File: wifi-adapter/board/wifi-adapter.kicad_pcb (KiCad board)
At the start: 2 copper layers, 25 x 24 mm, 17 parts, among them J1 DF13A-6P-1.25H, U1 LM1117IMPX-3.3, U2 ESP-07

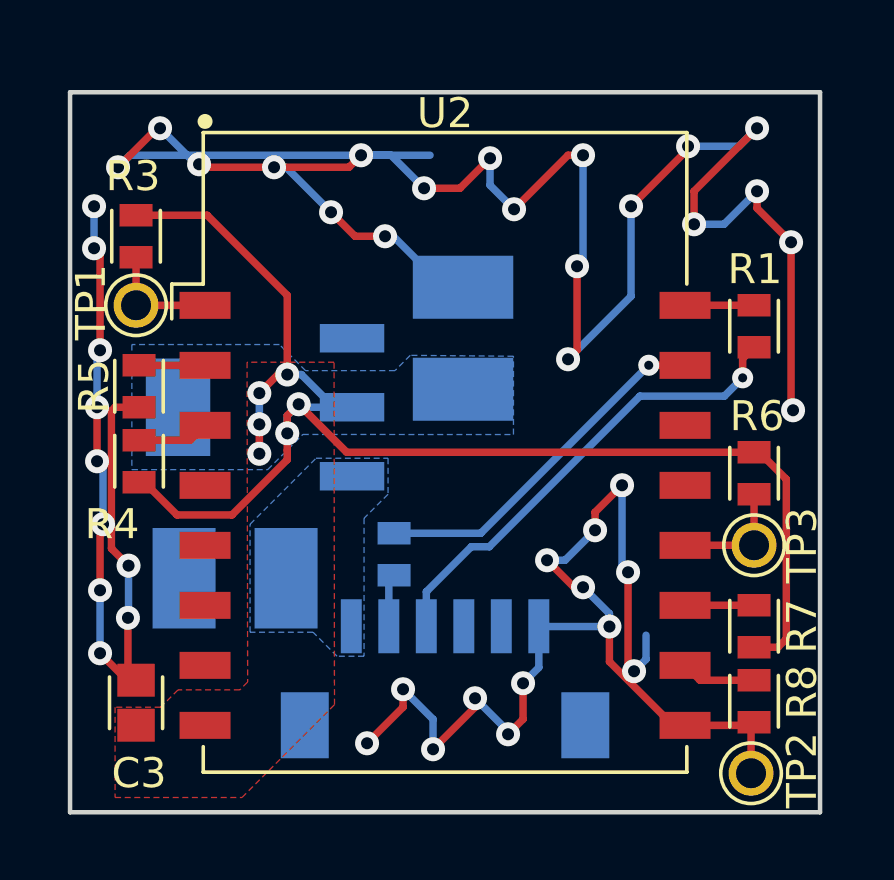
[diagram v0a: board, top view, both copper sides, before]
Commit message: Add GOST style schematic and gerber files
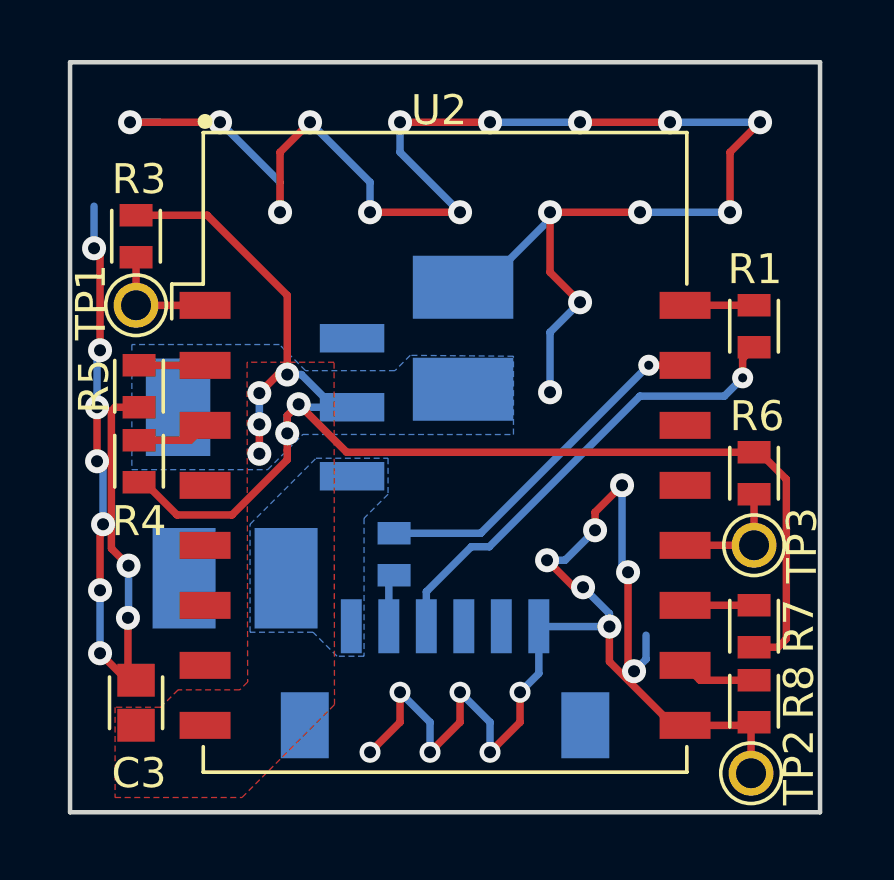
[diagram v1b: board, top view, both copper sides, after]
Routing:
- net GND: track 136.5 -> 122.3 mm, vias 43 -> 38
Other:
- board size 25 x 24 mm -> 25 x 25 mm

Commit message: Update to actual version
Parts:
- C1, C2: footprint spectrum:CAPC3225X230M -> wa:CAPC3225X230M
- C3: footprint spectrum:CAPC1608X92M -> wa:CAPC1608X92M
- J1: footprint spectrum:DF13A-6P-1.25H -> wa:HIROSE_DF13A-6P-1.25H
- R1, R2, R3, R4, R5, R6, R7, R8: footprint spectrum:RESC1608X55M -> wa:RESC1608X55M
- TP1, TP2, TP3: footprint spectrum:TP-TH-1 -> wa:TP-TH-1
- U1: footprint spectrum:SOT230P700X180-4M -> wa:SOT230P700X180-4M
- U2: footprint spectrum:SON200P2120X1600X300-16M -> wa:SON200P2120X1600X300-16M
- moved R2 1.04 mm to (147.7, 107.8), turned to 315 degrees
- moved R6 0.74 mm to (158.8, 105.0)
- moved R7 0.64 mm to (158.8, 110.2)
- moved TP3 0.55 mm to (158.8, 107.5)
- moved R4 0.46 mm to (138.3, 105.8)
- moved R3 0.29 mm to (138.2, 97.5)
- moved R8 0.19 mm to (158.8, 113.1)
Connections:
- J1 pad 4: Net-(J1-Pad4) -> (no net)
- J1 pad 5: Net-(J1-Pad5) -> (no net)
- J1 pad 7: Net-(J1-Pad7) -> (no net)
- J1 pad 8: Net-(J1-Pad8) -> (no net)
- U2 pad 13: Net-(U2-Pad13) -> (no net)
- U2 pad 14: Net-(U2-Pad14) -> (no net)
- U2 pad 4: Net-(U2-Pad4) -> (no net)
- U2 pad 5: Net-(U2-Pad5) -> (no net)
- U2 pad 6: Net-(U2-Pad6) -> (no net)
- U2 pad 7: Net-(U2-Pad7) -> (no net)
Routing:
- net GND: track 122.3 -> 131.5 mm, vias 38 -> 40
- net +3V3: track 49.5 -> 52.4 mm
- net Net-(R2-Pad2): track 12.0 -> 10.4 mm
- net /TELEM_TX: track 1.77 -> 2.61 mm

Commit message: Minor fixes in resistor values
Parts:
- R3, R5, R6, R7: value [NA] -> DNP
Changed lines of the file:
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@@
-(kicad_pcb (version 4) (host pcbnew 4.0.3+e1-6302~38~ubuntu16.04.1-stable)
+(kicad_pcb (version 4) (host pcbnew "(2015-10-14 BZR 6269)-product")
   (general
     (links 30)
@@
     (47 F.CrtYd user)
     (48 B.Fab user hide)
-    (49 F.Fab user hide)
+    (49 F.Fab user)
   )
   (setup
@@
       (effects (font (size 1 1) (thickness 0.12)))
     )
-    (fp_text value [NA] (at 0 0 90) (layer F.Fab)
+    (fp_text value DNP (at 0 0 90) (layer F.Fab)
       (effects (font (size 0.528 0.528) (thickness 0.1)))
     )
@@
       (effects (font (size 1 1) (thickness 0.12)))
     )
-    (fp_text value [NA] (at 0 0 270) (layer F.Fab)
+    (fp_text value DNP (at 0 0 270) (layer F.Fab)
       (effects (font (size 0.528 0.528) (thickness 0.1)))
     )
@@
       (effects (font (size 1 1) (thickness 0.12)))
     )
-    (fp_text value [NA] (at 0 0 270) (layer F.Fab)
+    (fp_text value DNP (at 0 0 270) (layer F.Fab)
       (effects (font (size 0.528 0.528) (thickness 0.1)))
     )
@@
       (effects (font (size 1 1) (thickness 0.12)))
     )
-    (fp_text value [NA] (at 0 0 90) (layer F.Fab)
-      (effects (font (size 0.528 0.528) (thickness 0.1)))
-    )
+    (fp_text value DNP (at 0 0 90) (layer F.Fab)
+      (effects (font (size 0.528 0.528) (thickness 0.1)))
+    )
